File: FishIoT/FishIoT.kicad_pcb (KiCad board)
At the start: 4 copper layers, 42 x 70 mm, 120 parts, among them IC1 RV-3032-C7_32.768KHZ-2.5PPM-T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, J1 USB4105-GF-A-120, J3 Conn_Coaxial, J4 BM05B-ZESS-TBT, J5 SF72S006VBDR2500, J6 Conn_Coaxial, J7 SHF-105-01-L-D-SM, J8 0705430001, SW1 PTS645SM43SMTR92 LF, SW2 PTS645SM43SMTR92 LF, SW3 PTS645SM43SMTR92 LF, U1 USBLC6-2P6, U2 NRF9151-LACA-R7, U3 CP2102N-Axx-xQFN20, U4 MAX-M10S, U5 TPD3F303DPVR, U6 MAX3471, U7 SI1040X-T1-GE3, U8 TPS63000, U9 RM126x

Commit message: Schematics cleanup
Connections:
- net /UART1_RX renamed /GNSS_UART_RX
- net /UART1_TX renamed /GNSS_UART_TX
- net /nRF_UART_RX renamed /USBC_UART_RX
- net /nRF_UART_TX renamed /USBC_UART_TX

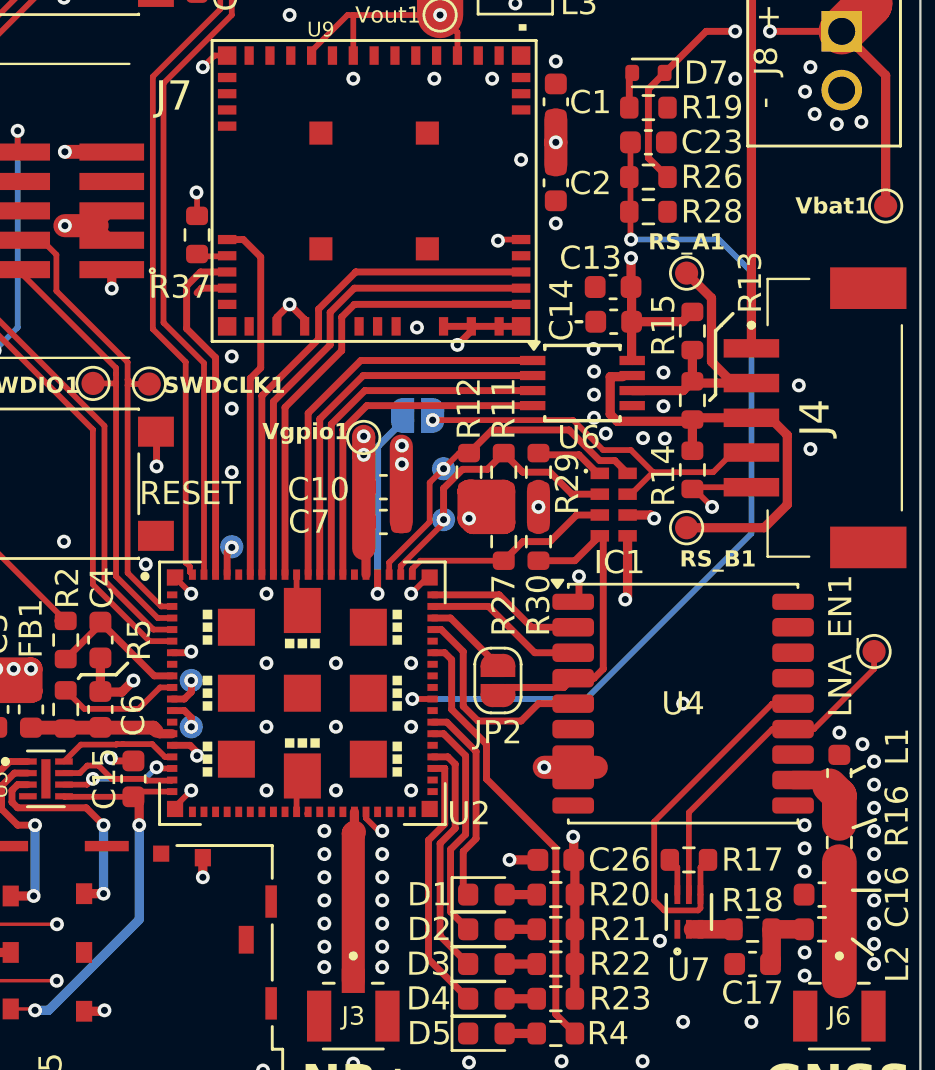
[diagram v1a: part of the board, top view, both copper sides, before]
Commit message: fixed battery measurement, DEC0 capacitor and I2C for GNSS
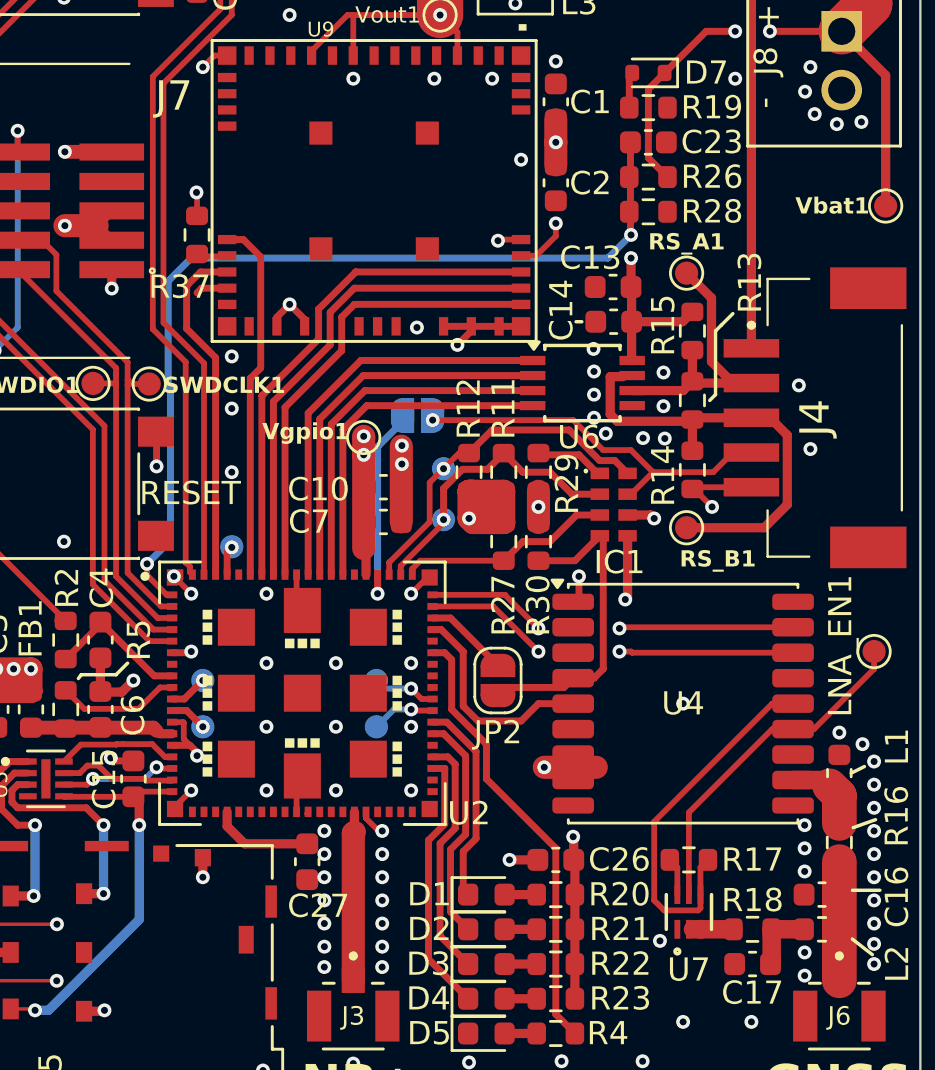
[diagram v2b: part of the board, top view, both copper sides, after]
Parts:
- added C27: 4.7uF, Capacitor_SMD:C_0603_1608Metric, F.Cu at (108.0, 88.1)
- added GPIO_P0.30: TestPoint, TestPoint:TestPoint_Pad_D1.0mm, B.Cu at (111.0, 82.2)
- added GPIO_P0.31: TestPoint, TestPoint:TestPoint_Pad_D1.0mm, B.Cu at (111.0, 80.2)
- moved GPIO_P.024 0.50 mm to (103.5, 80.2)
- moved GPIO_P.025 0.50 mm to (103.5, 82.2)
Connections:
- U2 pad 2: unconnected-(U2A-P0.20/AIN7-Pad2) -> /Battery_voltage
- U2 pad 24: unconnected-(U2A-DEC0-Pad24) -> Net-(U2A-DEC0)
- U2 pad 49: unconnected-(U2A-P0.30-Pad49) -> Net-(U2A-P0.30)
- U2 pad 50: /Battery_voltage -> Net-(U2A-P0.31)
- U2 pad 58: /GNSS_UART_RX -> /GNSS_SDA
- U2 pad 59: /GNSS_UART_TX -> /GNSS_SCL
- U4 pad 16: unconnected-(U4-SDA-Pad16) -> /GNSS_SDA
- U4 pad 17: unconnected-(U4-SCL-Pad17) -> /GNSS_SCL
- U4 pad 2: /GNSS_UART_TX -> unconnected-(U4-TXD-Pad2)
- U4 pad 3: /GNSS_UART_RX -> unconnected-(U4-RXD-Pad3)
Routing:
- net /GNSS_SDA: track 0.00 -> 16.4 mm, vias 0 -> 2
- net /GNSS_SCL: track 0.00 -> 16.2 mm, vias 0 -> 2
- net /GNSS_UART_RX: track 6.90 -> 0.00 mm
- net /GNSS_UART_TX: track 6.65 -> 0.00 mm
- net Net-(U2A-DEC0): track 0.00 -> 4.40 mm
- net GND: track 87.3 -> 91.3 mm
- net Net-(U2A-P0.31): track 0.00 -> 2.76 mm, vias 0 -> 1
- net Net-(U2A-P0.30): track 0.00 -> 2.76 mm, vias 0 -> 1
